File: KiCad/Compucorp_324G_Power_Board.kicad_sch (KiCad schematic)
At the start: 5 parts, among them J7 Power Interboard, J8 Power In, J9 To Scan Board

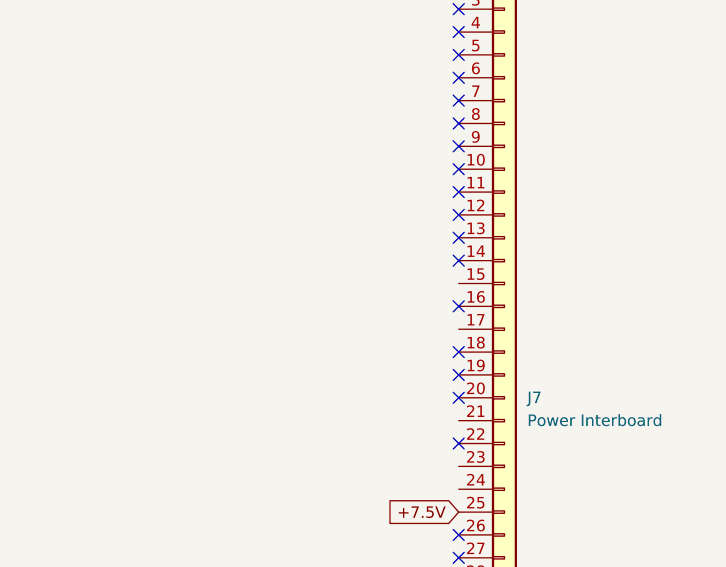
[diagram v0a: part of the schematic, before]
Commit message: Started Memory Board schematic
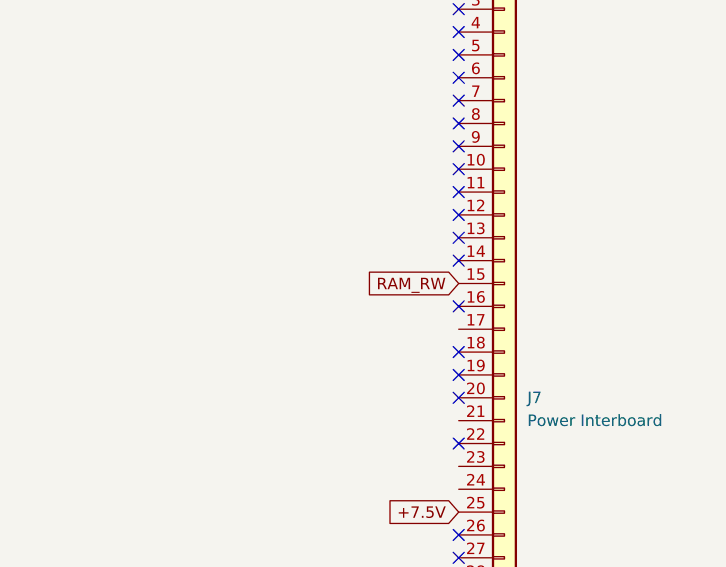
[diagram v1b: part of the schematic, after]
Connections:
- net RAM_RW: now reaches J7.15 (Pin_15)
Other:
- title: Compucorp 320-Series Power Board -> Compucorp 300-Series Power Board
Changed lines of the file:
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@@
 	(generator "eeschema")
 	(generator_version "9.0")
-	(paper "A4")
+	(paper "A3")
 	(title_block
-		(title "Compucorp 320-Series Power Board")
+		(title "Compucorp 300-Series Power Board")
 		(date "2/FEB/2026")
 		(rev "WIP")
@@
 			(effects
 				(font
+					(size 1.27 1.27)
+				)
+				(justify right)
+				(hide yes)
+			)
+		)
+	)
+	(global_label "RAM_RW"
+		(shape input)
+		(at 243.84 76.2 180)
+		(fields_autoplaced yes)
+		(effects
+			(font
+				(size 1.27 1.27)
+			)
+			(justify right)
+		)
+		(property "Intersheetrefs" "${INTERSHEET_REFS}"
+			(at 233.3558 76.2 0)
+			(effects
+				(font

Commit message: Memory board updates
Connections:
- net IB_33: now reaches J7.33 (Pin_33)
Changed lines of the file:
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@@
+		)
+	)
+	(global_label "IB_33"
+		(shape input)
+		(at 243.84 121.92 180)
+		(fields_autoplaced yes)
+		(effects
+			(font
+				(size 1.27 1.27)
+			)
+			(justify right)
+		)
+		(property "Intersheetrefs" "${INTERSHEET_REFS}"
+			(at 235.5934 121.92 0)
+			(effects
+				(font
+					(size 1.27 1.27)
+				)
+				(justify right)
+				(hide yes)
+			)
 		)
 	)

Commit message: Memory board updates
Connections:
- net RAM_RW: now also J7.23 (Pin_23); no longer J7.15 (Pin_15)
- net IB_17: now reaches J7.17 (Pin_17)
- new net IB_15: J7.15 (Pin_15)
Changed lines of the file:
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@@
+		)
+	)
+	(global_label "IB_15"
+		(shape input)
+		(at 243.84 76.2 180)
+		(fields_autoplaced yes)
+		(effects
+			(font
+				(size 1.27 1.27)
+			)
+			(justify right)
+		)
+		(property "Intersheetrefs" "${INTERSHEET_REFS}"
+			(at 235.5934 76.2 0)
+			(effects
+				(font
+					(size 1.27 1.27)
+				)
+				(justify right)
+				(hide yes)
+			)
 		)
 	)
@@
 		)
 	)
+	(global_label "+7.5V"
+		(shape input)
+		(at 157.48 124.46 180)
+		(fields_autoplaced yes)
+		(effects
+			(font
+				(size 1.27 1.27)
+			)
+			(justify right)
+		)
+		(property "Intersheetrefs" "${INTERSHEET_REFS}"
+			(at 148.81 124.46 0)
+			(effects
+				(font
+					(size 1.27 1.27)
+				)
+				(justify right)
+				(hide yes)
+			)
+		)
+	)
+	(global_label "-10V"
+		(shape input)
+		(at 243.84 127 180)
+		(fields_autoplaced yes)
+		(effects
+			(font
+				(size 1.27 1.27)
+			)
+			(justify right)
+		)
+		(property "Intersheetrefs" "${INTERSHEET_REFS}"
+			(at 235.7748 127 0)
+			(effects
+				(font
+					(size 1.27 1.27)
+				)
+				(justify right)
+				(hide yes)
+			)
+		)
+	)
+	(global_label "+5V"
+		(shape input)
+		(at 157.48 114.3 180)
+		(fields_autoplaced yes)
+		(effects
+			(font
+				(size 1.27 1.27)
+			)
+			(justify right)
+		)
+		(property "Intersheetrefs" "${INTERSHEET_REFS}"
+			(at 150.6243 114.3 0)
+			(effects
+				(font
+					(size 1.27 1.27)
+				)
+				(justify right)
+				(hide yes)
+			)
+		)
+	)
+	(global_label "+5V"
+		(shape input)
+		(at 243.84 124.46 180)
+		(fields_autoplaced yes)
+		(effects
+			(font
+				(size 1.27 1.27)
+			)
+			(justify right)
+		)
+		(property "Intersheetrefs" "${INTERSHEET_REFS}"
+			(at 236.9843 124.46 0)
+			(effects
+				(font
+					(size 1.27 1.27)
+				)
+				(justify right)
+				(hide yes)
+			)
+		)
+	)
+	(global_label "IB_17"
+		(shape input)
+		(at 243.84 81.28 180)
+		(fields_autoplaced yes)
+		(effects
+			(font
+				(size 1.27 1.27)
+			)
+			(justify right)
+		)
+		(property "Intersheetrefs" "${INTERSHEET_REFS}"
+			(at 235.5934 81.28 0)
+			(effects
+				(font
+					(size 1.27 1.27)
+				)
+				(justify right)
+				(hide yes)
+			)
+		)
+	)
+	(global_label "+7.5V"
+		(shape input)
+		(at 243.84 101.6 180)
+		(fields_autoplaced yes)
+		(effects
+			(font
+				(size 1.27 1.27)
+			)
+			(justify right)
+		)
+		(property "Intersheetrefs" "${INTERSHEET_REFS}"
+			(at 235.17 101.6 0)
+			(effects
+				(font
+					(size 1.27 1.27)
+				)
+				(justify right)
+				(hide yes)
+			)
+		)
+	)
+	(global_label "GND"
+		(shape input)
+		(at 243.84 132.08 180)
+		(fields_autoplaced yes)
+		(effects
+			(font
+				(size 1.27 1.27)
+			)
+			(justify right)
+		)
+		(property "Intersheetrefs" "${INTERSHEET_REFS}"
+			(at 236.9843 132.08 0)
+			(effects
+				(font
+					(size 1.27 1.27)
+				)
+				(justify right)
+				(hide yes)
+			)
+		)
+	)
 	(global_label "RAM_RW"
 		(shape input)
-		(at 243.84 76.2 180)
-		(fields_autoplaced yes)
-		(effects
-			(font
-				(size 1.27 1.27)
-			)
-			(justify right)
-		)
-		(property "Intersheetrefs" "${INTERSHEET_REFS}"
-			(at 233.3558 76.2 0)
-			(effects
-				(font
-					(size 1.27 1.27)
-				)
-				(justify right)
-				(hide yes)
-			)
-		)
-	)
-	(global_label "+7.5V"
-		(shape input)
-		(at 157.48 124.46 180)
-		(fields_autoplaced yes)
-		(effects
-			(font
-				(size 1.27 1.27)
-			)
-			(justify right)
-		)
-		(property "Intersheetrefs" "${INTERSHEET_REFS}"
-			(at 148.81 124.46 0)
-			(effects
-				(font
-					(size 1.27 1.27)
-				)
-				(justify right)
-				(hide yes)
-			)
-		)
-	)
-	(global_label "-10V"
-		(shape input)
-		(at 243.84 127 180)
-		(fields_autoplaced yes)
-		(effects
-			(font
-				(size 1.27 1.27)
-			)
-			(justify right)
-		)
-		(property "Intersheetrefs" "${INTERSHEET_REFS}"
-			(at 235.7748 127 0)
-			(effects
-				(font
-					(size 1.27 1.27)
-				)
-				(justify right)
-				(hide yes)
-			)
-		)
-	)
-	(global_label "+5V"
-		(shape input)
-		(at 157.48 114.3 180)
-		(fields_autoplaced yes)
-		(effects
-			(font
-				(size 1.27 1.27)
-			)
-			(justify right)
-		)
-		(property "Intersheetrefs" "${INTERSHEET_REFS}"
-			(at 150.6243 114.3 0)
-			(effects
-				(font
-					(size 1.27 1.27)
-				)
-				(justify right)
-				(hide yes)
-			)
-		)
-	)
-	(global_label "+5V"
-		(shape input)
-		(at 243.84 124.46 180)
-		(fields_autoplaced yes)
-		(effects
-			(font
-				(size 1.27 1.27)
-			)
-			(justify right)
-		)
-		(property "Intersheetrefs" "${INTERSHEET_REFS}"
-			(at 236.9843 124.46 0)
-			(effects
-				(font
-					(size 1.27 1.27)
-				)
-				(justify right)
-				(hide yes)
-			)
-		)
-	)
-	(global_label "+7.5V"
-		(shape input)
-		(at 243.84 101.6 180)
-		(fields_autoplaced yes)
-		(effects
-			(font
-				(size 1.27 1.27)
-			)
-			(justify right)
-		)
-		(property "Intersheetrefs" "${INTERSHEET_REFS}"
-			(at 235.17 101.6 0)
-			(effects
-				(font
-					(size 1.27 1.27)
-				)
-				(justify right)
-				(hide yes)
-			)
-		)
-	)
-	(global_label "GND"
-		(shape input)
-		(at 243.84 132.08 180)
-		(fields_autoplaced yes)
-		(effects
-			(font
-				(size 1.27 1.27)
-			)
-			(justify right)
-		)
-		(property "Intersheetrefs" "${INTERSHEET_REFS}"
-			(at 236.9843 132.08 0)
-			(effects
-				(font
+		(at 243.84 96.52 180)
+		(fields_autoplaced yes)
+		(effects
+			(font
+				(size 1.27 1.27)
+			)
+			(justify right)
+		)
+		(property "Intersheetrefs" "${INTERSHEET_REFS}"
+			(at 233.3558 96.52 0)
+			(effects
+				(font

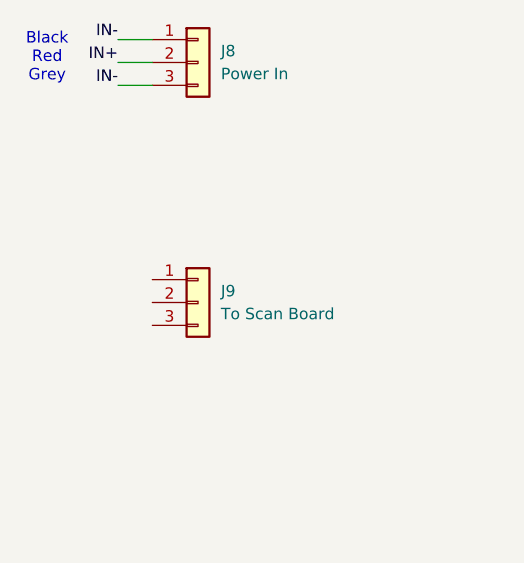
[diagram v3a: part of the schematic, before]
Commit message: Schematic updates
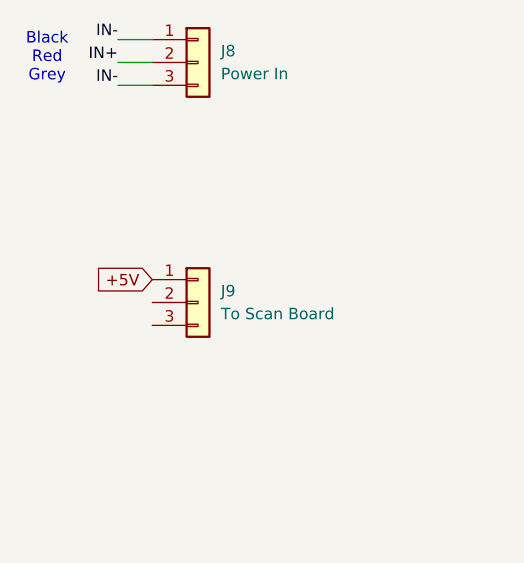
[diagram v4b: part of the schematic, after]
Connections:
- net +5V: now also J9.1 (Pin_1)
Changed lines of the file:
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@@
+	(global_label "+5V"
+		(shape input)
+		(at 41.91 60.96 180)
+		(fields_autoplaced yes)
+		(effects
+			(font
+				(size 1.27 1.27)
+			)
+			(justify right)
+		)
+		(property "Intersheetrefs" "${INTERSHEET_REFS}"
+			(at 35.0543 60.96 0)
+			(effects
+				(font
+					(size 1.27 1.27)
+				)
+				(justify right)
+				(hide yes)
+			)
+		)
+	)
 	(global_label "+5V"
 		(shape input)

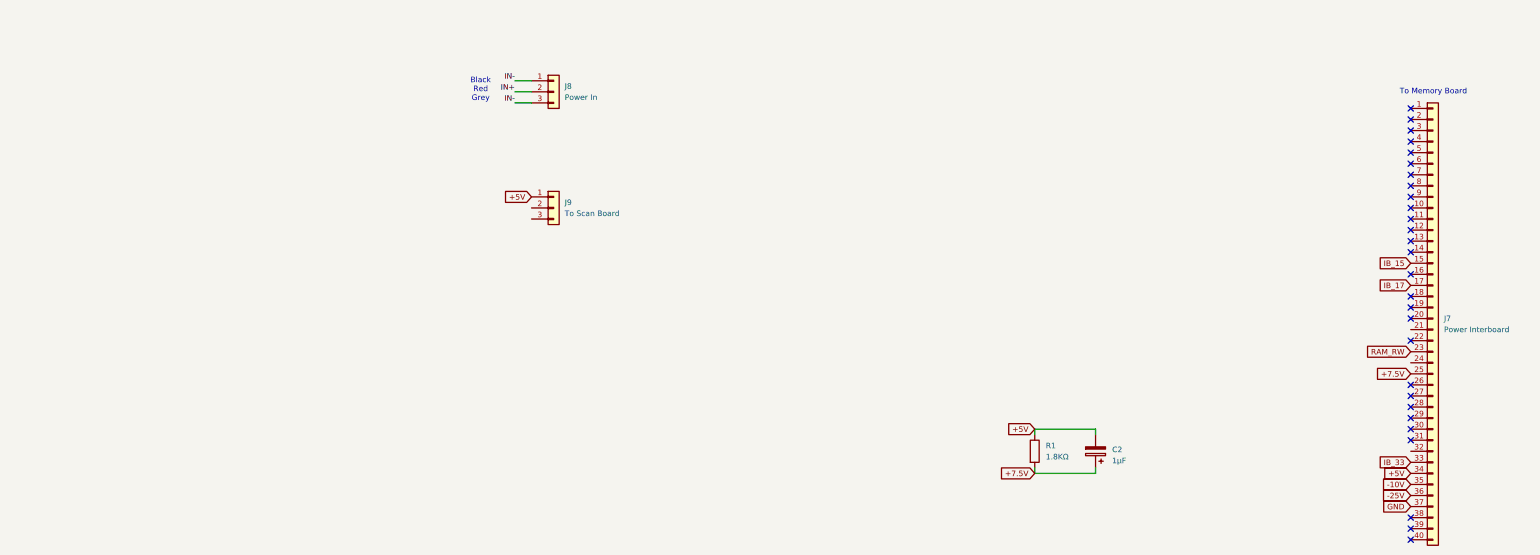
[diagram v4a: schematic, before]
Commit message: Update Compucorp_324G_Power_Board.kicad_sch
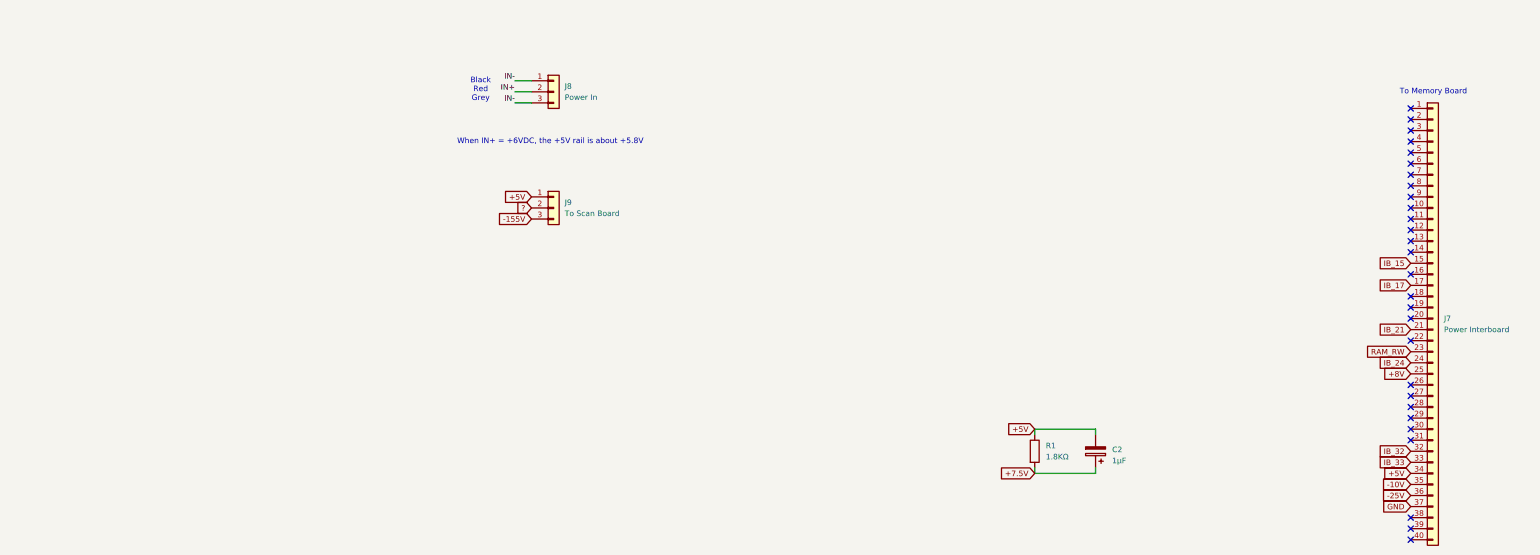
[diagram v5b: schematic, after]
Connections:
- net +7.5V: no longer J7.25 (Pin_25)
- net IB_21: now reaches J7.21 (Pin_21)
- net IB_24: now reaches J7.24 (Pin_24)
- net IB_32: now reaches J7.32 (Pin_32)
- net ?: now reaches J9.2 (Pin_2)
- net -155V: now reaches J9.3 (Pin_3)
- new net +8V: J7.25 (Pin_25)
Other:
- note added: "When IN+ = +6VDC, the +5V rail is about +5.8V"
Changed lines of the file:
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@@
 		(company "Brett Hallen")
+	)
+	(text "When IN+ = +6VDC, the +5V rail is about +5.8V"
+		(exclude_from_sim no)
+		(at 46.228 48.26 0)
+		(effects
+			(font
+				(size 1.27 1.27)
+			)
+		)
 	)
 	(text "Black\nRed\nGrey"
@@
 		)
 	)
+	(global_label "IB_24"
+		(shape input)
+		(at 243.84 99.06 180)
+		(fields_autoplaced yes)
+		(effects
+			(font
+				(size 1.27 1.27)
+			)
+			(justify right)
+		)
+		(property "Intersheetrefs" "${INTERSHEET_REFS}"
+			(at 235.5934 99.06 0)
+			(effects
+				(font
+					(size 1.27 1.27)
+				)
+				(justify right)
+				(hide yes)
+			)
+		)
+	)
 	(global_label "+7.5V"
 		(shape input)
@@
 		)
 	)
-	(global_label "+7.5V"
+	(global_label "+8V"
 		(shape input)
 		(at 243.84 101.6 180)
@@
 		)
 		(property "Intersheetrefs" "${INTERSHEET_REFS}"
-			(at 235.17 101.6 0)
+			(at 236.9843 101.6 0)
+			(effects
+				(font
+					(size 1.27 1.27)
+				)
+				(justify right)
+				(hide yes)
+			)
+		)
+	)
+	(global_label "?"
+		(shape input)
+		(at 41.91 63.5 180)
+		(fields_autoplaced yes)
+		(effects
+			(font
+				(size 1.27 1.27)
+			)
+			(justify right)
+		)
+		(property "Intersheetrefs" "${INTERSHEET_REFS}"
+			(at 37.8362 63.5 0)
 			(effects
 				(font
@@
 		)
 	)
+	(global_label "IB_32"
+		(shape input)
+		(at 243.84 119.38 180)
+		(fields_autoplaced yes)
+		(effects
+			(font
+				(size 1.27 1.27)
+			)
+			(justify right)
+		)
+		(property "Intersheetrefs" "${INTERSHEET_REFS}"
+			(at 235.5934 119.38 0)
+			(effects
+				(font
+					(size 1.27 1.27)
+				)
+				(justify right)
+				(hide yes)
+			)
+		)
+	)
+	(global_label "IB_21"
+		(shape input)
+		(at 243.84 91.44 180)
+		(fields_autoplaced yes)
+		(effects
+			(font
+				(size 1.27 1.27)
+			)
+			(justify right)
+		)
+		(property "Intersheetrefs" "${INTERSHEET_REFS}"
+			(at 235.5934 91.44 0)
+			(effects
+				(font
+					(size 1.27 1.27)
+				)
+				(justify right)
+				(hide yes)
+			)
+		)
+	)
 	(global_label "RAM_RW"
 		(shape input)
@@
 			(effects
 				(font
+					(size 1.27 1.27)
+				)
+				(justify right)
+				(hide yes)
+			)
+		)
+	)
+	(global_label "-155V"
+		(shape input)
+		(at 41.91 66.04 180)
+		(fields_autoplaced yes)
+		(effects
+			(font
+				(size 1.27 1.27)
+			)
+			(justify right)
+		)
+		(property "Intersheetrefs" "${INTERSHEET_REFS}"
+			(at 32.6353 66.04 0)
+			(effects
+				(font

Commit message: Update Compucorp_324G_Power_Board.kicad_sch
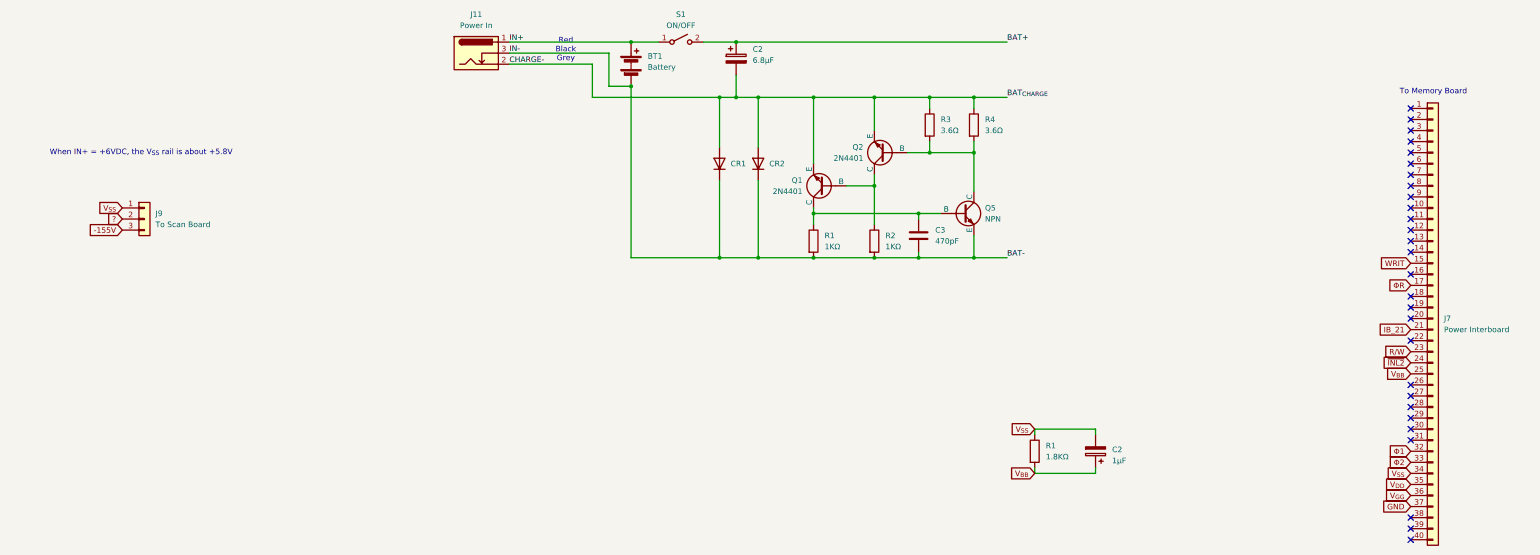
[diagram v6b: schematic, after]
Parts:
- removed J8: Power In, symbol Connector_Generic:Conn_01x03
- added BT1: Battery, symbol Device:Battery
- added C2: 6.8µF, symbol Device:C_Polarized
- added C3: 470pF, symbol Device:C
- added CR1, CR2: D, symbol Device:D
- added J11: Power In, symbol Connector:Barrel_Jack_Switch
- added Q1, Q2: 2N4401, symbol Simulation_SPICE:NPN
- added Q5: NPN, symbol Simulation_SPICE:NPN
- added R1, R2: 1KΩ, symbol Device:R
- added R3, R4: 3.6Ω, symbol Device:R
- added S1: ON/OFF, symbol Switch:SW_SPST
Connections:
- net +8V is gone; now on net V_{BB}: J7.25 (Pin_25)
- net IN+: now also BT1.1 (+), J11.1, S1.1 (A)
- net +5V renamed V_{SS}
- net +7.5V renamed V_{BB}
- net -10V renamed V_{DD}
- net -25V renamed V_{GG}
- net IB_15 renamed WRIT
- net IB_17 renamed ΦR
- net IB_24 renamed ~{INL2}
- net IB_32 renamed Φ1
- net IB_33 renamed Φ2
- net RAM_RW renamed R/W
- new net: Q1.2 (B), Q2.1 (C), R2.1
- new net: Q2.2 (B), Q5.1 (C), R3.2, R4.2
- new net: C3.1, Q1.1 (C), Q5.2 (B), R1.1
- new net BAT+: C2.1, S1.2 (B)
- new net BAT-: BT1.2 (-), C3.2, CR1.1 (K), CR2.1 (K), J11.3, Q5.3 (E), R1.2, R2.2
- new net BAT_{CHARGE}: C2.2, CR1.2 (A), CR2.2 (A), J11.2, Q1.3 (E), Q2.3 (E), R3.1, R4.1
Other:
- note added: "Red Black Grey"
- note added: "When IN+ = +6VDC, the V_{SS} rail is about +5.8V"
- note removed: "Black Red Grey"
- note removed: "When IN+ = +6VDC, the +5V rail is about +5.8V"
- moved on the sheet: J9
